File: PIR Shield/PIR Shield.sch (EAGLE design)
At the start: 11 parts, among them IC1 MC33269T-5.0, J1 POWER_JACKPTH

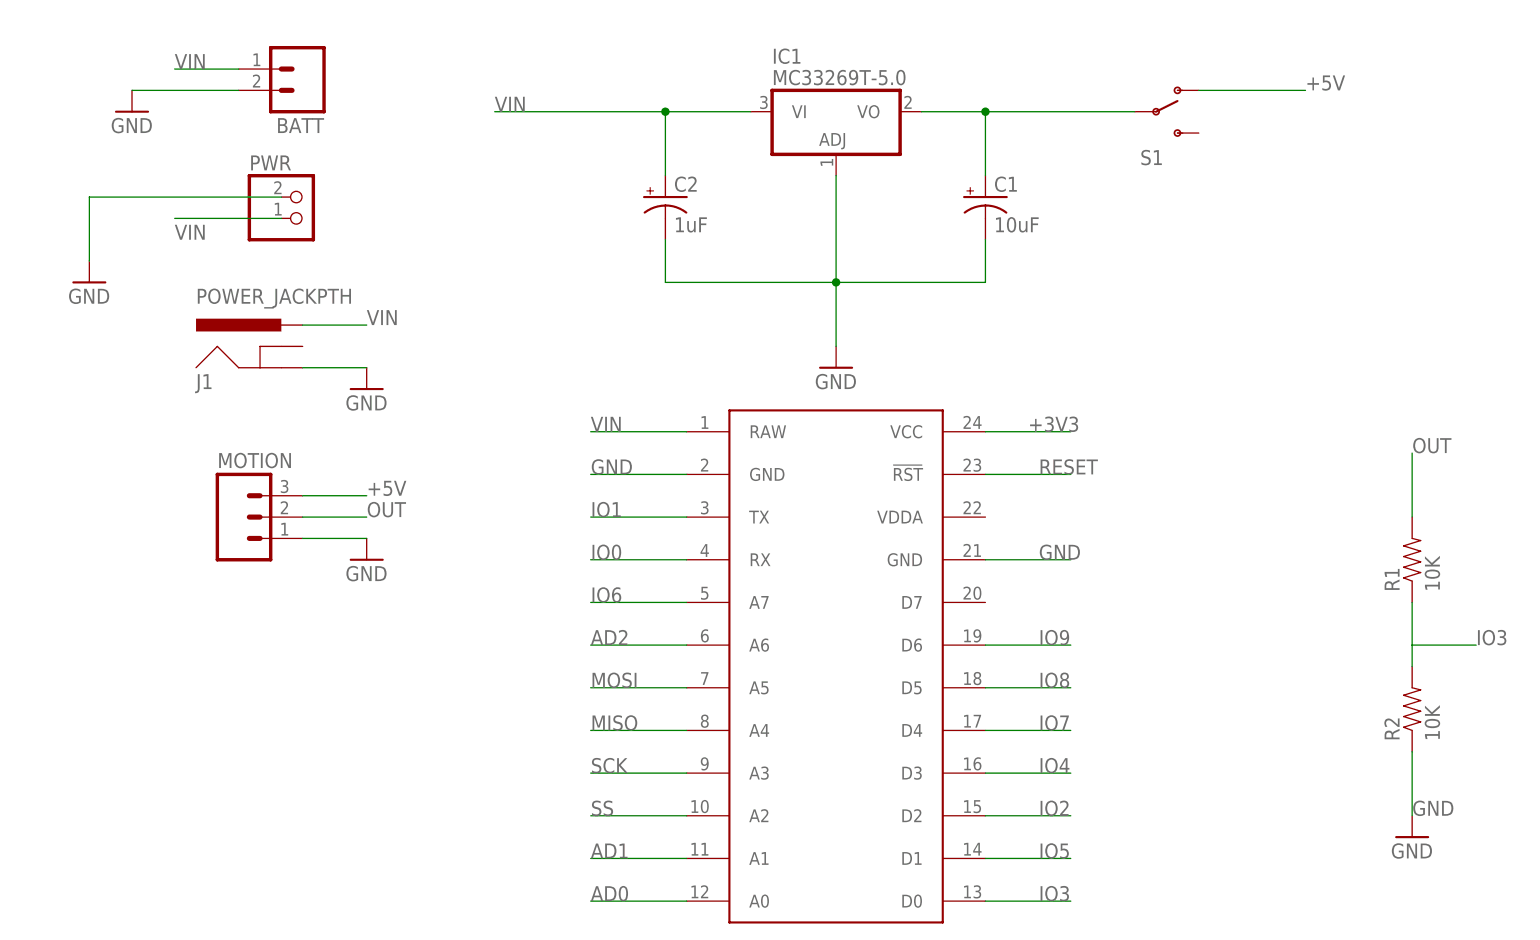
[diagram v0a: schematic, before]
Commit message: Reviewed battery shield and PIR shield. Good to go.
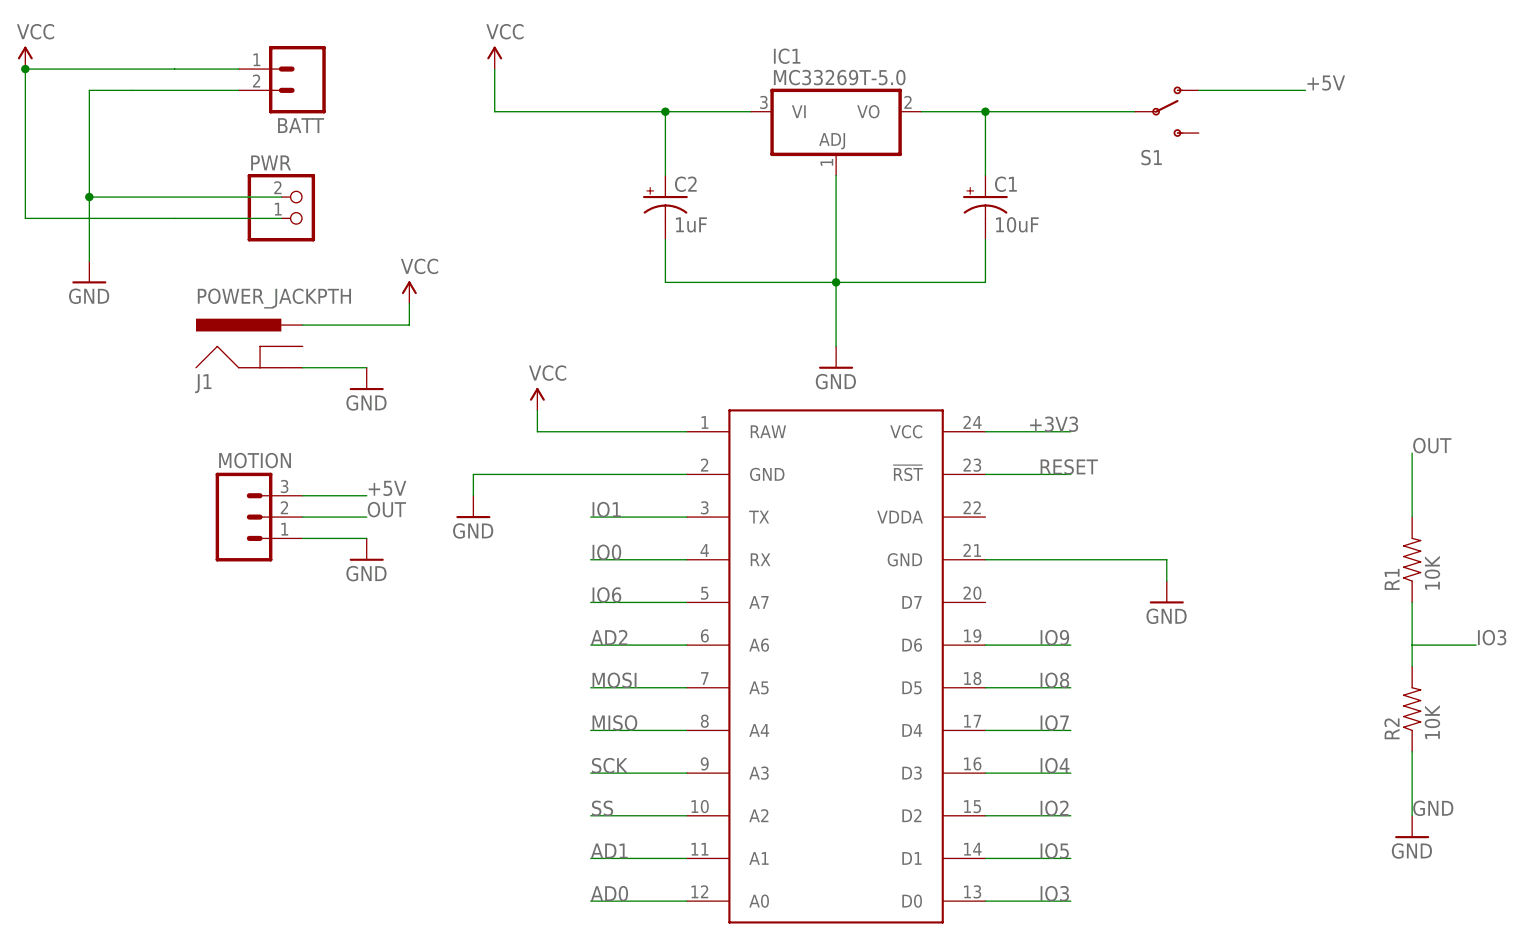
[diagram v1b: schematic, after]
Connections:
- net VIN renamed VCC
